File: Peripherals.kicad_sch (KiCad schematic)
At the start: 12 parts, among them U1 SHT4x

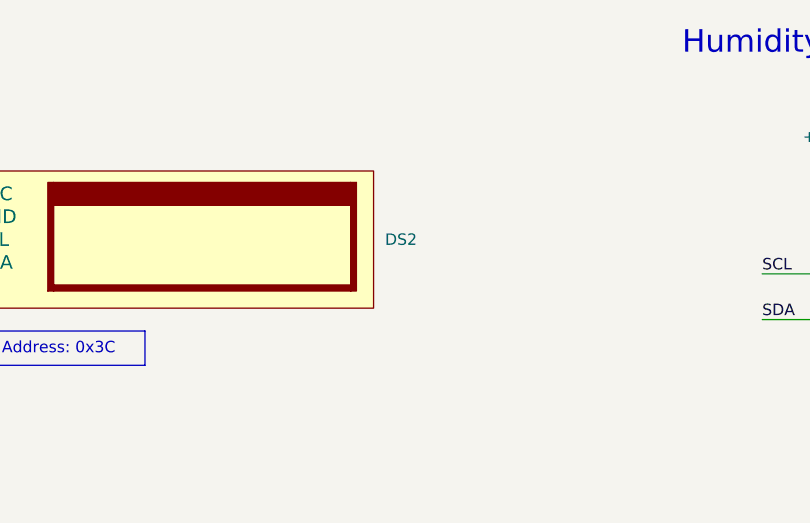
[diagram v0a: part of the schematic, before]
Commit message: Added FPGA oscillator, made FPGA sheet larger
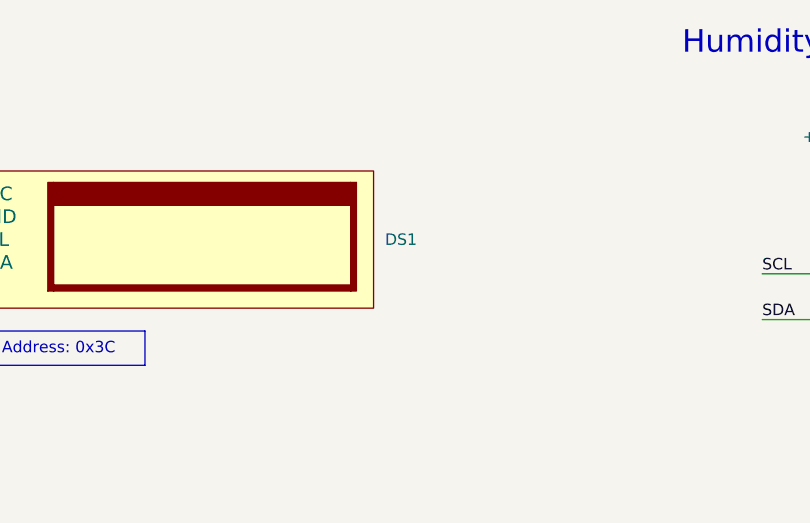
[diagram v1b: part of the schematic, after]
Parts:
- renumbered DS2 to DS1
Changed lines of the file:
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@@
   (symbol (lib_id "LEDs & Displays:DS_MIDAS_MDOB128064V2V-WI") (at 116.84 80.01 0) (unit 1)
     (in_bom yes) (on_board yes) (dnp no) (fields_autoplaced)
-    (property "Reference" "DS2" (at 163.83 87.63 0)
+    (property "Reference" "DS1" (at 163.83 87.63 0)
       (effects (font (size 1.27 1.27)) (justify left))
     )

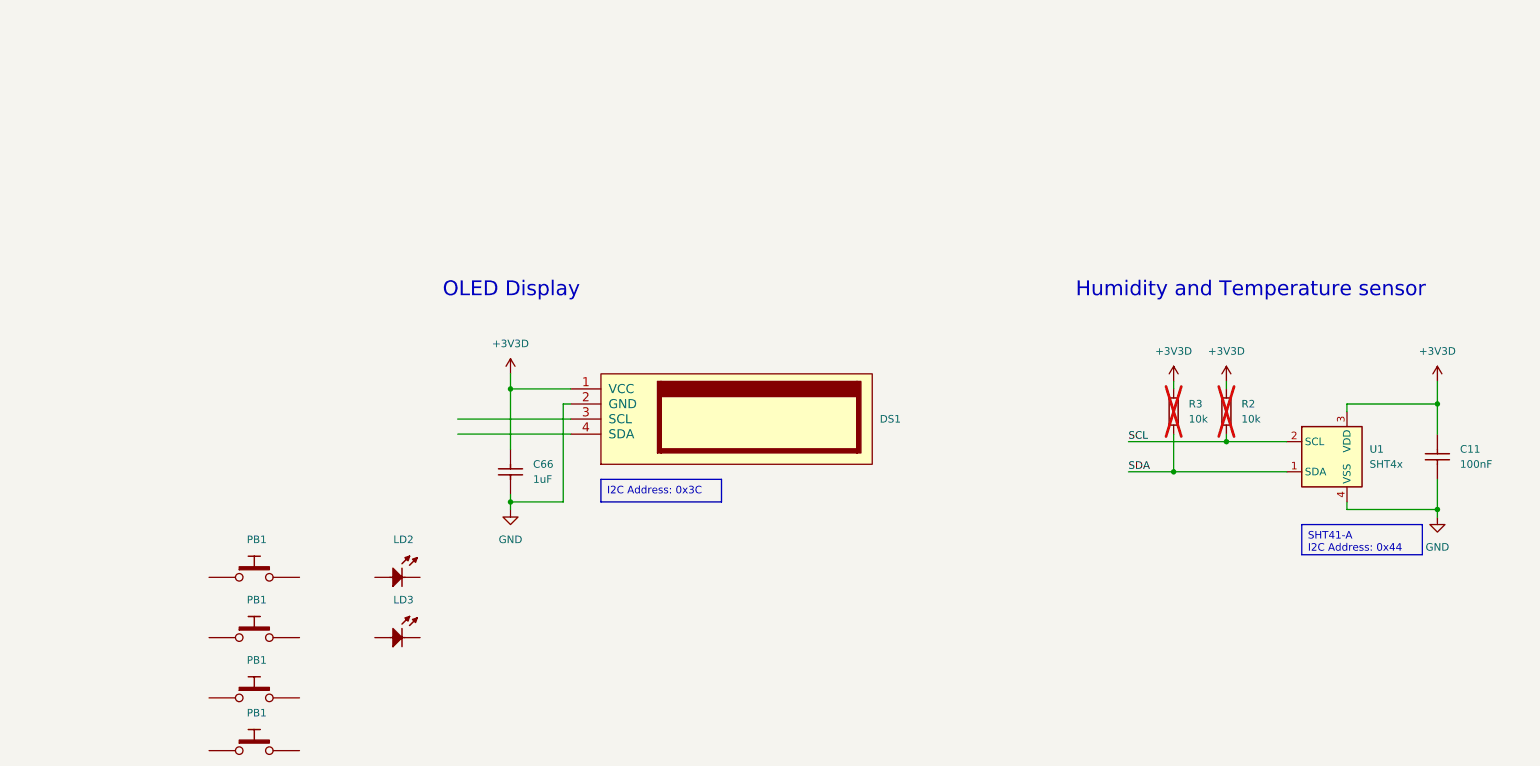
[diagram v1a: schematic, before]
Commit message: Connected FPGA to Accurate, added Atsam, fixed some Accurate connections
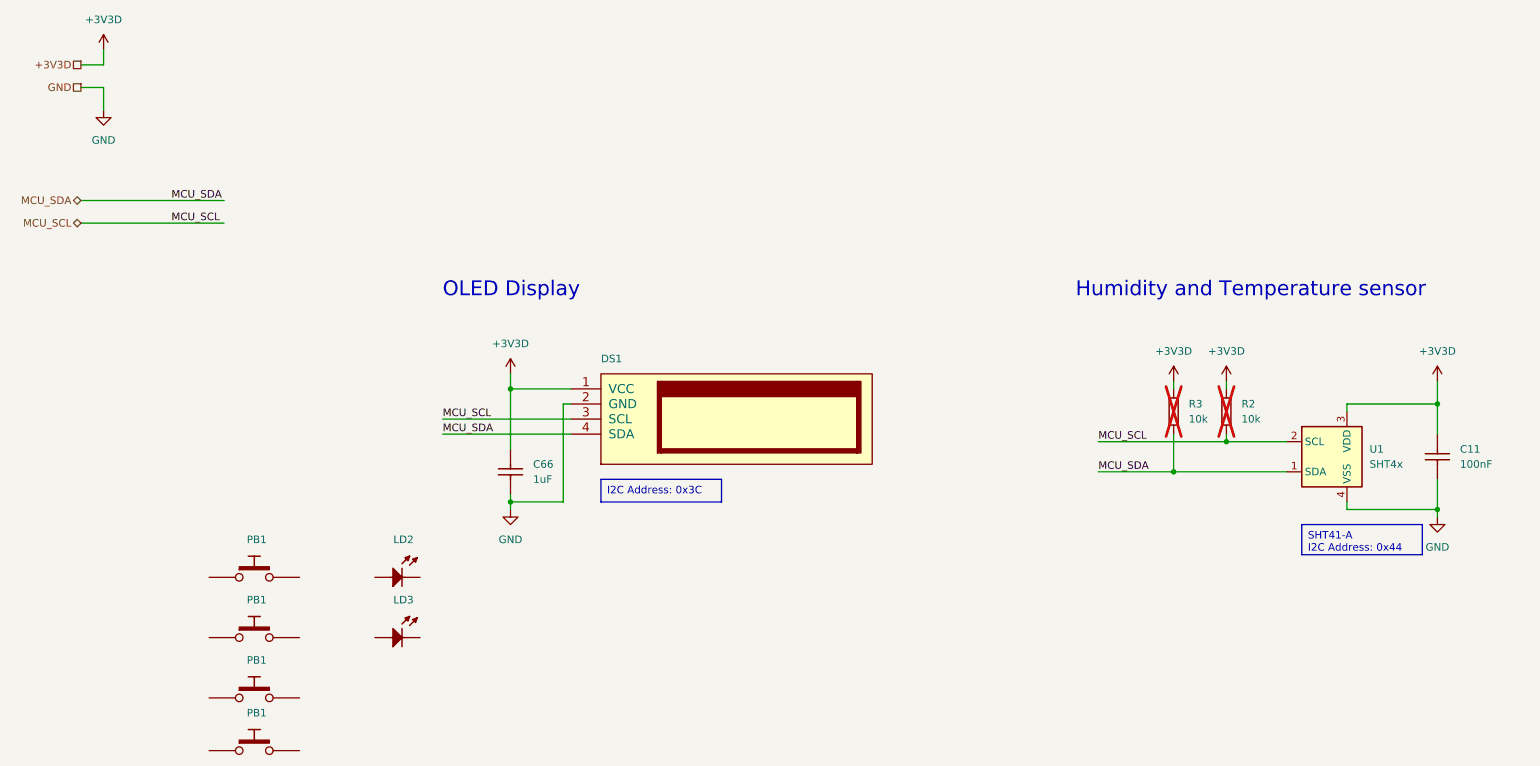
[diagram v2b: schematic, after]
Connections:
- net SCL is gone; now on net MCU_SCL: R2.1, U1.2 (SCL)
- net SDA is gone; now on net MCU_SDA: R3.1, U1.1 (SDA)
- net MCU_SCL: now reaches DS1.3 (SCL)
- net MCU_SDA: now reaches DS1.4 (SDA)
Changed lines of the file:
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@@
 (kicad_sch (version 20230121) (generator eeschema)
-  (paper "A4")
+  (paper "A3")
   (junction (at 101.6 82.55) (diameter 0) (color 0 0 0 0)
   )
@@
     (stroke (width 0) (type default))
   )
-  (wire (pts (xy 92.71 87.63) (xy 111.76 87.63))
-    (stroke (width 0) (type default))
-  )
-  (wire (pts (xy 92.71 90.17) (xy 111.76 90.17))
+  (wire (pts (xy 90.17 87.63) (xy 111.76 87.63))
+    (stroke (width 0) (type default))
+  )
+  (wire (pts (xy 90.17 90.17) (xy 111.76 90.17))
     (stroke (width 0) (type default))
   )
@@
     (stroke (width 0) (type default))
   )
+  (wire (pts (xy 29.21 27.94) (xy 33.02 27.94))
+    (stroke (width 0) (type default))
+  )
+  (wire (pts (xy 29.21 50.8) (xy 53.34 50.8))
+    (stroke (width 0) (type default))
+  )
   (wire (pts (xy 222.25 91.44) (xy 222.25 90.17))
     (stroke (width 0) (type default))
@@
     (stroke (width 0) (type default))
   )
-  (wire (pts (xy 205.74 96.52) (xy 213.36 96.52))
+  (wire (pts (xy 200.66 96.52) (xy 213.36 96.52))
     (stroke (width 0) (type default))
   )
@@
     (stroke (width 0) (type default))
   )
-  (wire (pts (xy 205.74 91.44) (xy 222.25 91.44))
+  (wire (pts (xy 200.66 91.44) (xy 222.25 91.44))
     (stroke (width 0) (type default))
   )
@@
     (stroke (width 0) (type default))
   )
+  (wire (pts (xy 33.02 27.94) (xy 33.02 25.4))
+    (stroke (width 0) (type default))
+  )
   (wire (pts (xy 257.81 102.87) (xy 257.81 104.14))
     (stroke (width 0) (type default))
@@
     (stroke (width 0) (type default))
   )
+  (wire (pts (xy 29.21 31.75) (xy 33.02 31.75))
+    (stroke (width 0) (type default))
+  )
   (wire (pts (xy 242.57 102.87) (xy 257.81 102.87))
     (stroke (width 0) (type default))
@@
     (stroke (width 0) (type default))
   )
+  (wire (pts (xy 29.21 54.61) (xy 53.34 54.61))
+    (stroke (width 0) (type default))
+  )
   (wire (pts (xy 101.6 101.6) (xy 101.6 102.87))
+    (stroke (width 0) (type default))
+  )
+  (wire (pts (xy 33.02 31.75) (xy 33.02 35.56))
     (stroke (width 0) (type default))
   )
@@
     (effects (font (size 2.5 2.5)) (justify left bottom))
   )
-  (label "SDA" (at 205.74 96.52 0) (fields_autoplaced)
+  (label "MCU_SDA" (at 90.17 90.17 0) (fields_autoplaced)
     (effects (font (size 1.27 1.27)) (justify left bottom))
   )
-  (label "SCL" (at 205.74 91.44 0) (fields_autoplaced)
+  (label "MCU_SCL" (at 44.45 54.61 0) (fields_autoplaced)
     (effects (font (size 1.27 1.27)) (justify left bottom))
+  )
+  (label "MCU_SDA" (at 44.45 50.8 0) (fields_autoplaced)
+    (effects (font (size 1.27 1.27)) (justify left bottom))
+  )
+  (label "MCU_SCL" (at 90.17 87.63 0) (fields_autoplaced)
+    (effects (font (size 1.27 1.27)) (justify left bottom))
+  )
+  (label "MCU_SDA" (at 200.66 96.52 0) (fields_autoplaced)
+    (effects (font (size 1.27 1.27)) (justify left bottom))
+  )
+  (label "MCU_SCL" (at 200.66 91.44 0) (fields_autoplaced)
+    (effects (font (size 1.27 1.27)) (justify left bottom))
+  )
+  (hierarchical_label "MCU_SCL" (shape bidirectional) (at 29.21 54.61 180) (fields_autoplaced)
+    (effects (font (size 1.27 1.27)) (justify right))
+  )
+  (hierarchical_label "+3V3D" (shape passive) (at 29.21 27.94 180) (fields_autoplaced)
+    (effects (font (size 1.27 1.27)) (justify right))
+  )
+  (hierarchical_label "GND" (shape passive) (at 29.21 31.75 180) (fields_autoplaced)
+    (effects (font (size 1.27 1.27)) (justify right))
+  )
+  (hierarchical_label "MCU_SDA" (shape bidirectional) (at 29.21 50.8 180) (fields_autoplaced)
+    (effects (font (size 1.27 1.27)) (justify right))
   )
   (symbol (lib_id "Resistors SMD:R0805_10K_0.1%_0.1W_10PPM") (at 222.25 90.17 90) (unit 1)
@@
     )
   )
+  (symbol (lib_id "symbol_lib:+3V3D") (at 33.02 25.4 0) (unit 1)
+    (in_bom yes) (on_board yes) (dnp no) (fields_autoplaced)
+    (property "Reference" "#PWR032" (at 33.02 29.21 0)
+      (effects (font (size 1.27 1.27)) hide)
+    )
+    (property "Value" "+3V3D" (at 33.02 20.32 0)
+      (effects (font (size 1.27 1.27)))
+    )
+    (property "Footprint" "" (at 33.02 25.4 0)
+      (effects (font (size 1.27 1.27)) hide)
+    )
+    (property "Datasheet" "" (at 33.02 25.4 0)
+      (effects (font (size 1.27 1.27)) hide)
+    )
+    (pin "1")
+    (instances
+      (project "Accurate_Eval"
+        (path "/d3b6a045-fd77-42ad-b330-1b1925488537/929e0cdf-f54c-4a28-a6d4-8b706822a456"
+          (reference "#PWR032") (unit 1)
+        )
+        (path "/d3b6a045-fd77-42ad-b330-1b1925488537/c6a8b2ea-c0f0-4c02-aeaa-57ac874f0dd5"
+          (reference "#PWR0120") (unit 1)
+        )
+        (path "/d3b6a045-fd77-42ad-b330-1b1925488537/59667e70-bb75-464b-9655-2a4f5dbb3db0"
+          (reference "#PWR0122") (unit 1)
+        )
+      )
+    )
+  )
   (symbol (lib_id "LEDs & Displays:DS_MIDAS_MDOB128064V2V-WI") (at 116.84 80.01 0) (unit 1)
-    (in_bom yes) (on_board yes) (dnp no) (fields_autoplaced)
-    (property "Reference" "DS1" (at 163.83 87.63 0)
+    (in_bom yes) (on_board yes) (dnp no)
+    (property "Reference" "DS1" (at 116.84 77.47 0)
       (effects (font (size 1.27 1.27)) (justify left))
     )
@@
         )
       )
+    )
+  )
+  (symbol (lib_id "power:GND") (at 33.02 35.56 0) (unit 1)
+    (in_bom yes) (on_board yes) (dnp no) (fields_autoplaced)
+    (property "Reference" "#PWR031" (at 33.02 41.91 0)
+      (effects (font (size 1.27 1.27)) hide)
+    )
+    (property "Value" "GND" (at 33.02 40.64 0)
+      (effects (font (size 1.27 1.27)))
+    )
+    (property "Footprint" "" (at 33.02 35.56 0)
+      (effects (font (size 1.27 1.27)) hide)
+    )
+    (property "Datasheet" "" (at 33.02 35.56 0)
+      (effects (font (size 1.27 1.27)) hide)
+    )
+    (pin "1")
+    (instances
+      (project "Accurate_Eval"
+        (path "/d3b6a045-fd77-42ad-b330-1b1925488537/929e0cdf-f54c-4a28-a6d4-8b706822a456"
+          (reference "#PWR031") (unit 1)
+        )
+        (path "/d3b6a045-fd77-42ad-b330-1b1925488537/c6a8b2ea-c0f0-4c02-aeaa-57ac874f0dd5"
+          (reference "#PWR0121") (unit 1)
+        )
+        (path "/d3b6a045-fd77-42ad-b330-1b1925488537/59667e70-bb75-464b-9655-2a4f5dbb3db0"
+          (reference "#PWR0149") (unit 1)
+        )
+      )

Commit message: Made MCU schematic, made root schematic, adding ESD diodes, fixed  EDR errors
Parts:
- removed LD2: LED_LITEON_LTST-C193KRKT-5A, ICs And Semiconductors SMD:LED_LITEON_LTST-C193KRKT-5A, symbol LEDs & Displays:LED_LITEON_LTST-C193KRKT-5A
- removed LD3: LED_LITEON_LTST-C193KSKT-5A, ICs And Semiconductors SMD:LED_LITEON_LTST-C193KSKT-5A, symbol LEDs & Displays:LED_LITEON_LTST-C193KSKT-5A
- removed PB1 (x4): PB_C&K_KSC321JLFS, Switches:PB_C&K_KSC321J, symbol Switches:PB_C&K_KSC321JLFS
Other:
- note added: "Inputs"
- note added: "Power Ports"
- moved on the sheet: C11, C66, DS1, R2, R3, U1

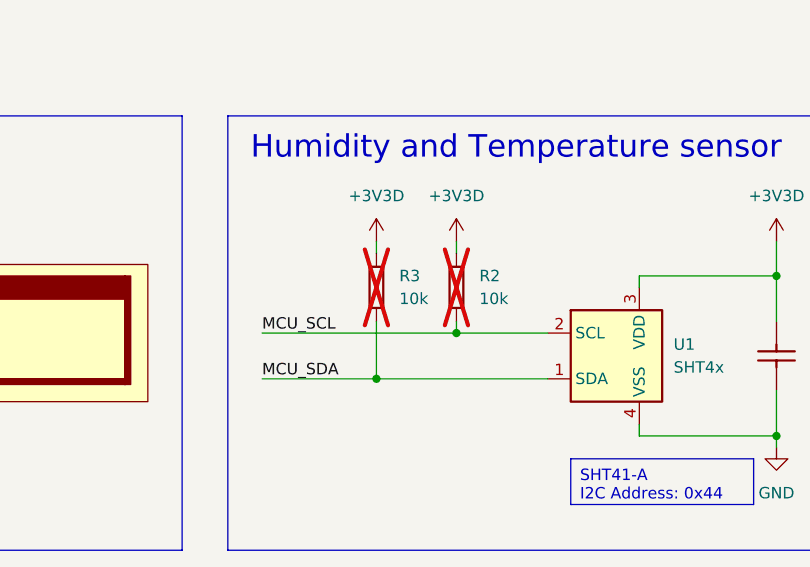
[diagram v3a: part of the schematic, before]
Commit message: Added triax connector, added test points, fixed some mistakes
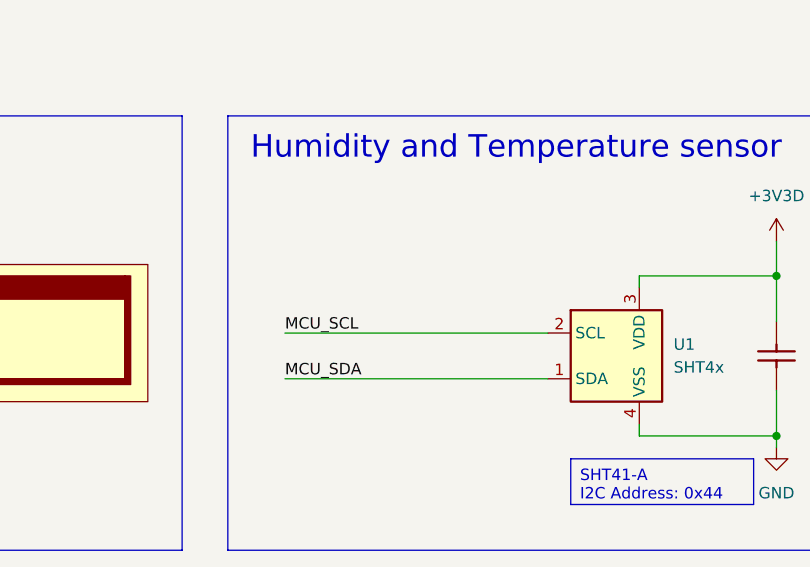
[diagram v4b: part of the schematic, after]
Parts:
- removed R2, R3: R0805_10K_0.1%_0.1W_10PPM, Resistors SMD:RESC2012X60N, symbol Resistors SMD:R0805_10K_0.1%_0.1W_10PPM
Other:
- company: (none) -> CERN
- title: (none) -> ACCURATE 2 Evaluation Board

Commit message: Polished the schematic a bit
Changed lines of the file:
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@@
-    (stroke (width 0) (type default))
-  )
-  (polyline (pts (xy 53.3146 107.4166) (xy 53.3146 109.2962))
     (stroke (width 0) (type default))
   )
@@
     (stroke (width 0) (type default))
   )
-  (wire (pts (xy 227.33 45.72) (xy 227.33 49.53))
+  (wire (pts (xy 227.33 48.26) (xy 227.33 49.53))
     (stroke (width 0) (type default))
   )
@@
     (effects (font (size 1.27 1.27)) (justify right))
   )
-  (symbol (lib_id "symbol_lib:+3V3D") (at 227.33 45.72 0) (unit 1)
+  (symbol (lib_id "symbol_lib:+3V3D") (at 227.33 48.26 0) (unit 1)
     (in_bom yes) (on_board yes) (dnp no) (fields_autoplaced)
-    (property "Reference" "#PWR016" (at 227.33 49.53 0)
+    (property "Reference" "#PWR016" (at 227.33 52.07 0)
       (effects (font (size 1.27 1.27)) hide)
     )
-    (property "Value" "+3V3D" (at 227.33 40.64 0)
+    (property "Value" "+3V3D" (at 227.33 43.18 0)
       (effects (font (size 1.27 1.27)))
     )
-    (property "Footprint" "" (at 227.33 45.72 0)
+    (property "Footprint" "" (at 227.33 48.26 0)
       (effects (font (size 1.27 1.27)) hide)
     )
-    (property "Datasheet" "" (at 227.33 45.72 0)
+    (property "Datasheet" "" (at 227.33 48.26 0)
       (effects (font (size 1.27 1.27)) hide)
     )
